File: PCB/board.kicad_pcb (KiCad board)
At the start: 2 copper layers, 161 parts, among them J1 Micro_SD_Card, J10 Conn_01x10, J11 Conn_01x02, J12 Conn_02x04_Odd_Even, J13 Conn_01x02, J14 Conn_01x02, J15 Conn_01x03, J16 Conn_01x02, J17 Conn_01x05, J18 Conn_01x04, J19 Conn_01x04, J2 Conn_ARM_JTAG_SWD_10, J20 Conn_01x02, J21 Conn_01x03, J22 Conn_02x04_Odd_Even, J23 Conn_01x04, J24 Conn_01x04, J25 Conn_01x02, J26 Conn_01x03, J27 Conn_02x04_Odd_Even, J28 Conn_01x04, J29 Conn_01x04, J3 USB_C_Receptacle_USB2.0_14P, J30 Conn_01x02, J31 Conn_01x03, J32 Conn_01x02, J33 Conn_01x02, J34 Conn_01x02, J35 Conn_01x02, J36 Conn_01x02, J37 Conn_01x02, J4 Conn_01x04, J5 Conn_01x04, J6 Conn_01x02, J7 Conn_01x03, J8 Conn_02x04_Odd_Even, J9 Conn_01x10, Q1 IRLML6402, Q2 NMOS, Q3 NMOS, Q4 NMOS, Q5 NMOS, Q6 NMOS, SW1 SW_Push, SW2 SW_Push, U1 STM32H743VITx, U2 AP7361C, U4 TMC Stepstick, U5 TMC Stepstick, U6 TMC Stepstick, U7 TMC Stepstick, U8 AP63203WU, Y2 25 MHz

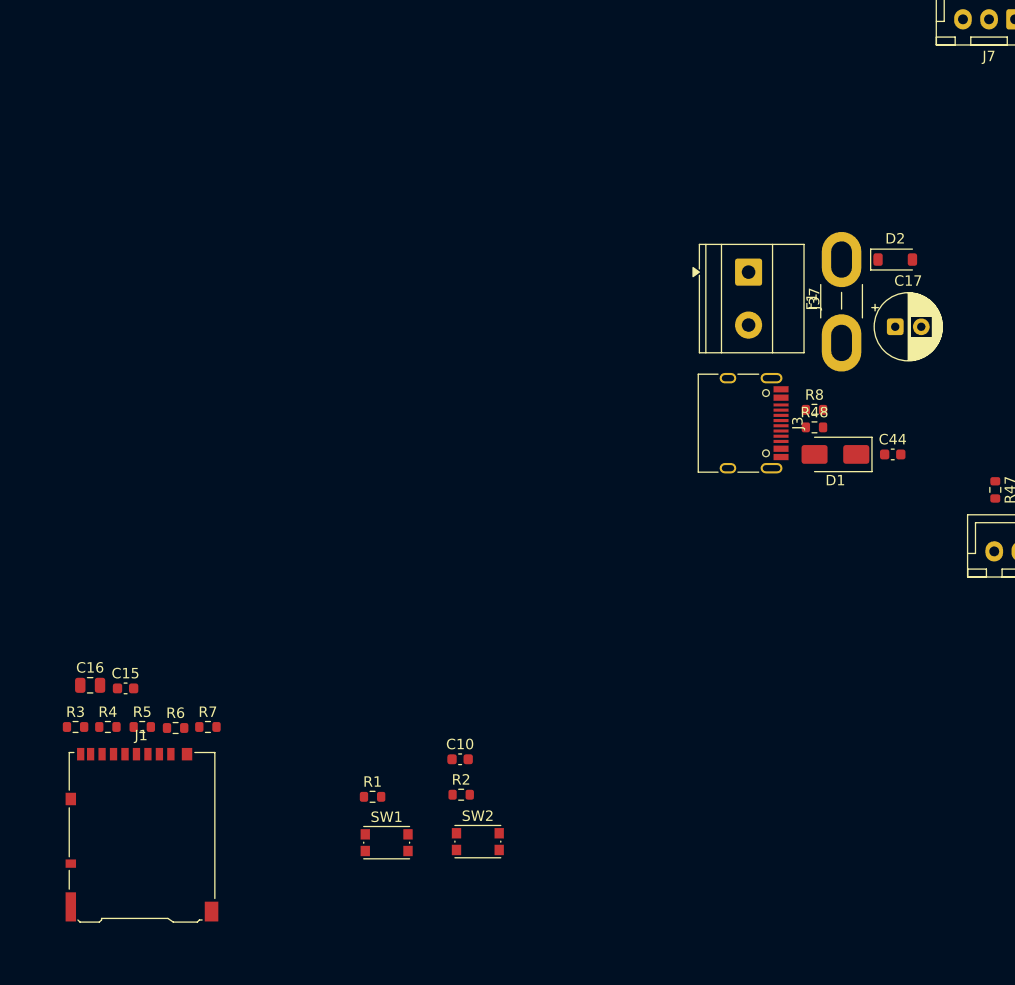
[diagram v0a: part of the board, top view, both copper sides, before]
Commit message: much better organization of the pcb
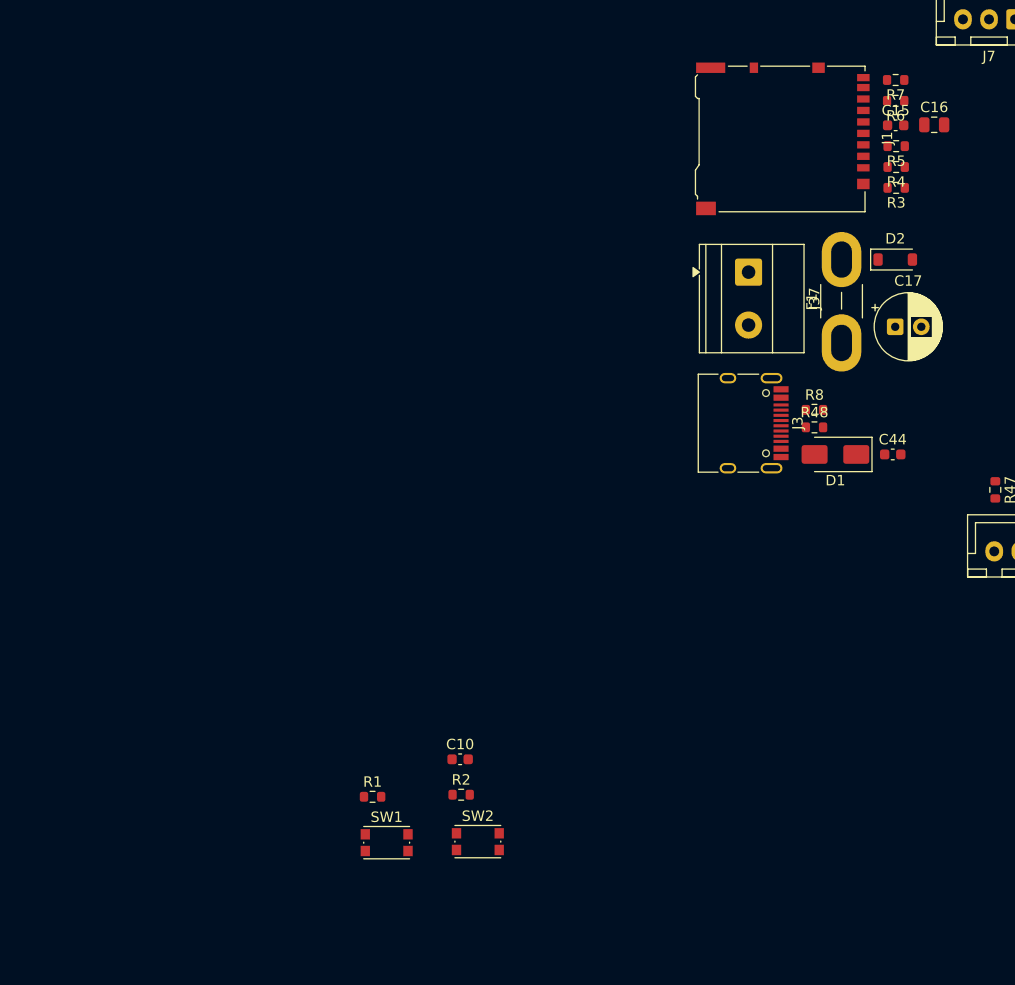
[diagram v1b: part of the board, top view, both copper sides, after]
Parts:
- moved C16 97.2 mm to (159.0, 80.0)
- moved R3 94.2 mm to (155.3, 86.1), turned to 180 degrees
- moved R4 92.8 mm to (155.3, 84.1), turned to 180 degrees
- moved R6 91.6 mm to (155.3, 77.7), turned to 180 degrees
- moved C15 91.5 mm to (155.3, 80.1)
- moved R5 91.3 mm to (155.3, 82.1), turned to 180 degrees
- moved J1 90.8 mm to (144.5, 81.4), turned to -90 degrees
- moved R7 90.6 mm to (155.3, 75.7), turned to 180 degrees

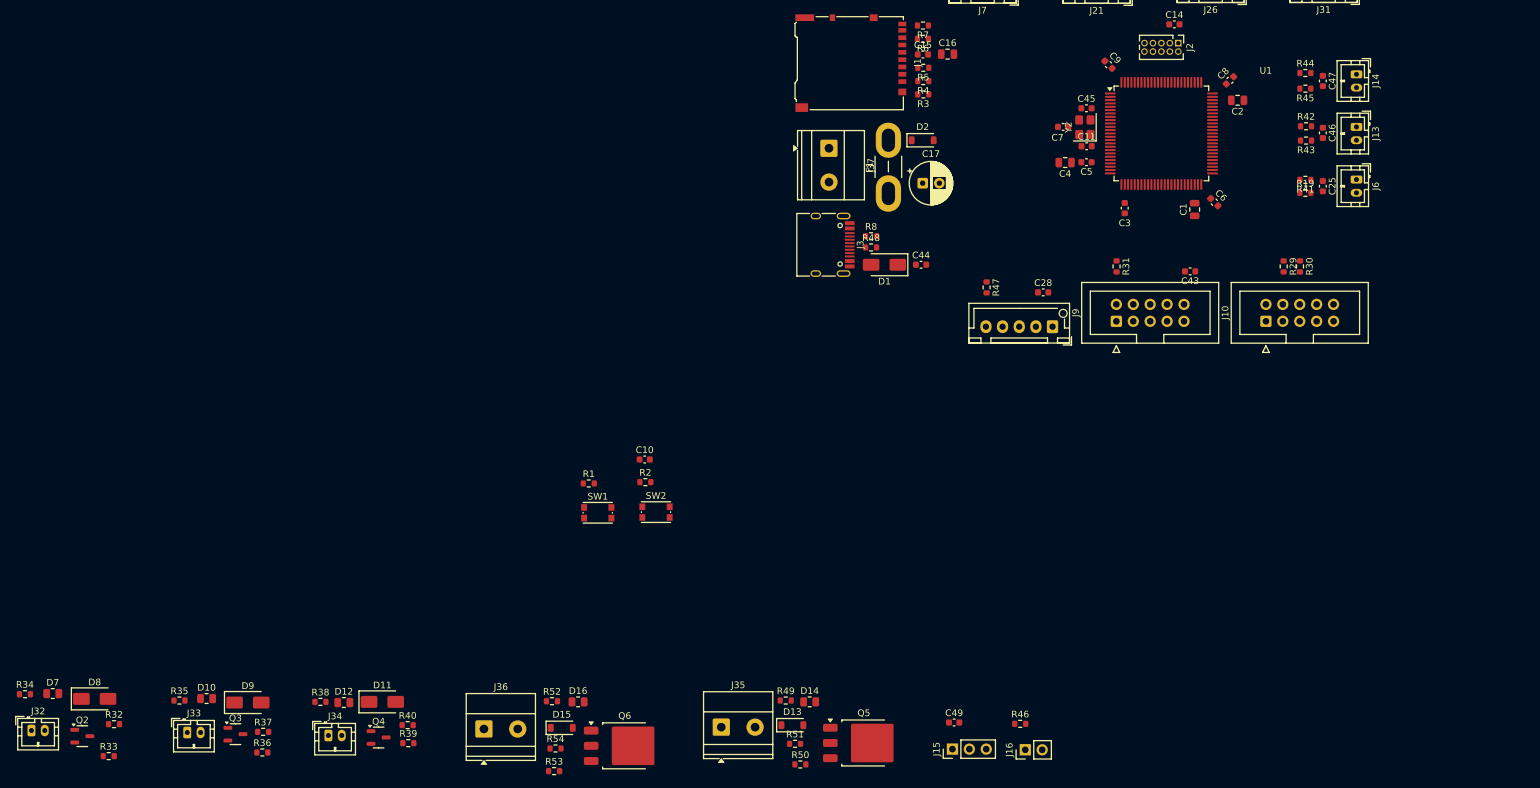
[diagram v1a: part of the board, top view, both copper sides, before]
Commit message: organized fan connectors
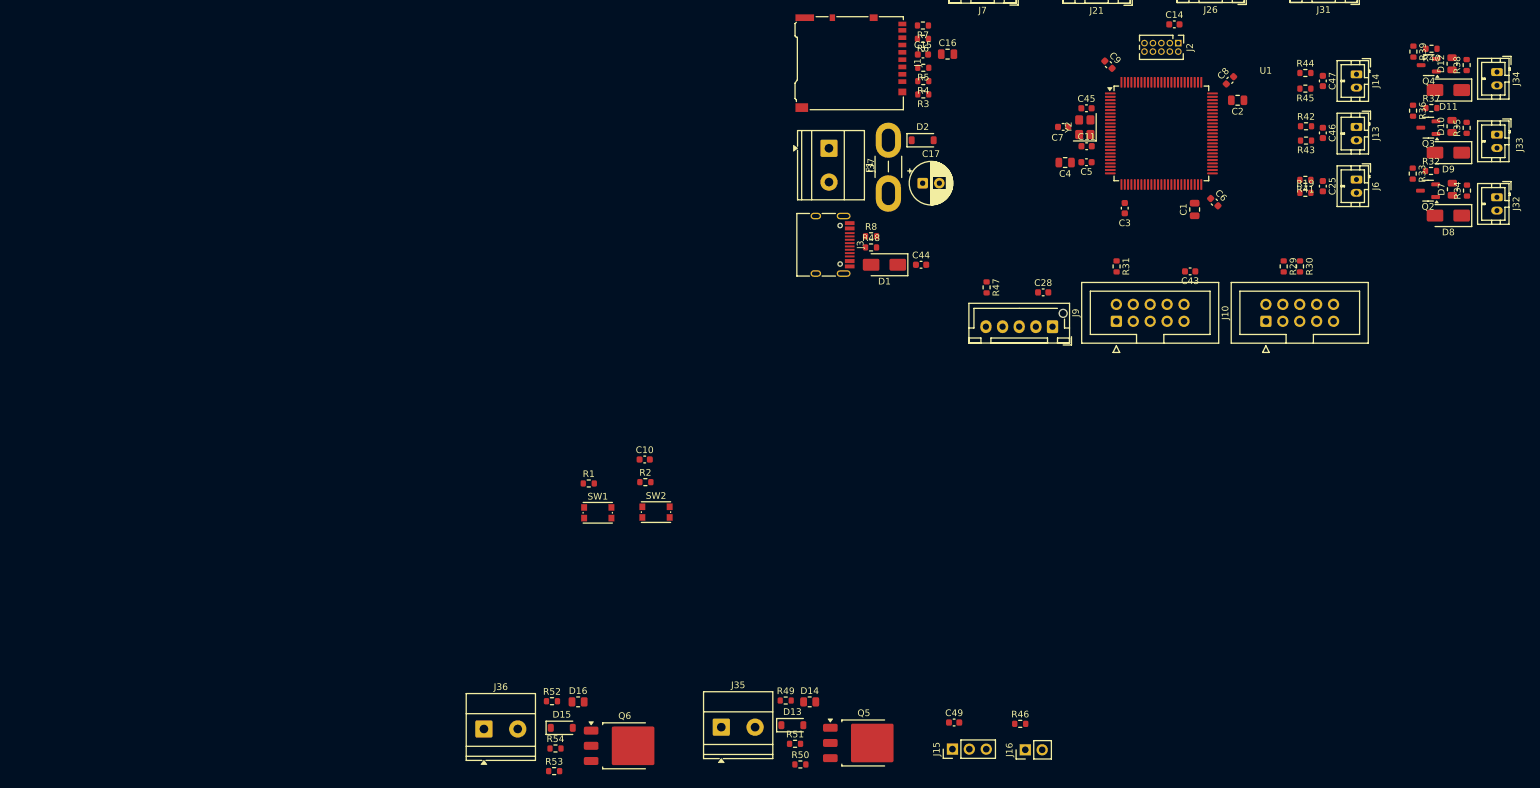
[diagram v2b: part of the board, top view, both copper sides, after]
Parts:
- moved J32 234.2 mm to (241.5, 101.5), turned to -90 degrees
- moved R34 229.4 mm to (237.0, 100.5), turned to 90 degrees
- moved D7 223.4 mm to (234.8, 100.3), turned to 90 degrees
- moved Q2 218.1 mm to (231.2, 100.5), turned to 180 degrees
- moved J33 216.2 mm to (241.5, 92.1), turned to -90 degrees
- moved D8 215.9 mm to (234.2, 104.3), turned to 180 degrees
- moved R32 214.5 mm to (231.6, 97.6)
- moved R33 214.5 mm to (228.8, 98.0), turned to -90 degrees
- moved R35 211.6 mm to (236.9, 91.1), turned to 90 degrees
- moved D10 205.8 mm to (234.8, 90.9), turned to 90 degrees
- moved J34 201.8 mm to (241.5, 82.7), turned to -90 degrees
- moved Q3 201.0 mm to (231.2, 91.1), turned to 180 degrees
- moved R37 198.9 mm to (231.7, 88.1)
- moved D9 198.3 mm to (234.2, 94.8), turned to 180 degrees
- moved R36 197.9 mm to (228.9, 88.5), turned to -90 degrees
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
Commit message: heaters
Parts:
- D13: footprint Diode_SMD:D_SOD-123 -> Diode_SMD:D_SMA
- D15: footprint Diode_SMD:D_SOD-123 -> Package_TO_SOT_SMD:TO-263-2
- moved SW1 76.2 mm to (170.7, 107.8)
- moved C10 71.6 mm to (174.8, 103.8), turned to -90 degrees
- moved SW2 71.5 mm to (170.7, 103.8)
- moved R1 71.4 mm to (165.9, 107.2), turned to 180 degrees
- moved R2 66.7 mm to (165.9, 103.0)
- moved Q6 38.6 mm to (91.8, 150.1), turned to 90 degrees
- moved R53 30.7 mm to (93.2, 157.8)
- moved R54 28.3 mm to (90.3, 157.8)
- moved Q5 19.2 mm to (137.4, 166.5), turned to 90 degrees
- moved D16 19.1 mm to (84.5, 174.7), turned to 180 degrees
- moved D15 18.2 mm to (91.9, 165.4), turned to 90 degrees
- moved R52 14.9 mm to (85.5, 172.2), turned to -90 degrees
- moved R50 10.4 mm to (139.3, 176.6)
- moved R51 10.0 mm to (139.2, 174.1), turned to 180 degrees
- moved J35 8.30 mm to (132.9, 183.5)
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
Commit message: all components place all organized
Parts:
- moved J36 188.9 mm to (269.3, 123.9), turned to 90 degrees
- moved D16 183.9 mm to (262.6, 128.7), turned to -90 degrees
- moved R52 180.2 mm to (260.1, 127.8), turned to 0 degrees
- moved D15 167.4 mm to (253.3, 121.3), turned to 180 degrees
- moved R54 159.3 mm to (245.7, 123.0), turned to 90 degrees
- moved R53 157.1 mm to (245.7, 120.0), turned to 90 degrees
- moved J35 154.1 mm to (269.3, 111.7), turned to 90 degrees
- moved Q6 149.0 mm to (238.0, 121.5), turned to 180 degrees
- moved R49 143.7 mm to (262.3, 109.3), turned to 90 degrees
- moved R50 142.1 mm to (262.3, 105.4), turned to 90 degrees
- moved D13 141.6 mm to (259.5, 113.0), turned to 180 degrees
- moved J15 140.8 mm to (237.9, 67.3), turned to 180 degrees
- moved D14 140.6 mm to (260.1, 109.1), turned to 90 degrees
- moved C49 138.9 mm to (234.9, 63.4), turned to -90 degrees
- moved R51 138.8 mm to (259.9, 105.4), turned to -90 degrees
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
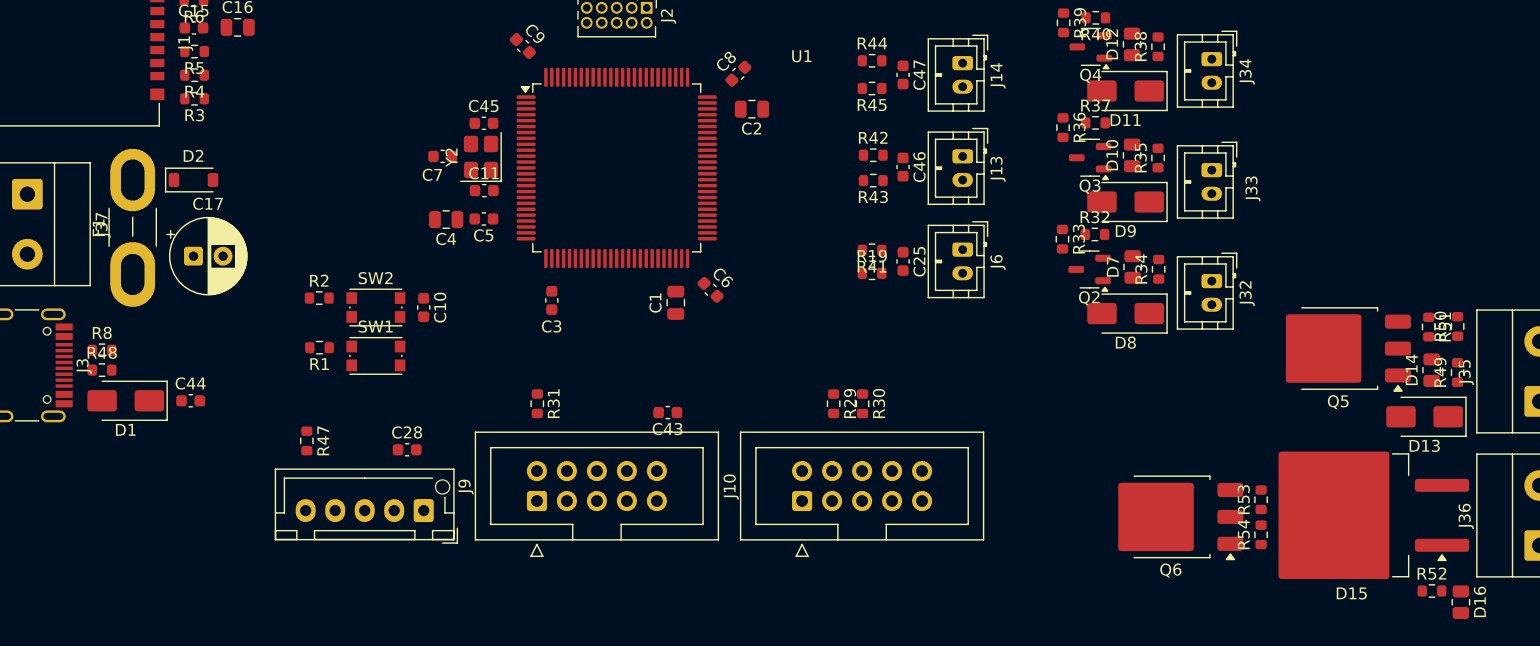
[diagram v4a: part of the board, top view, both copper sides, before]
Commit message: added the organization stuff to the journal
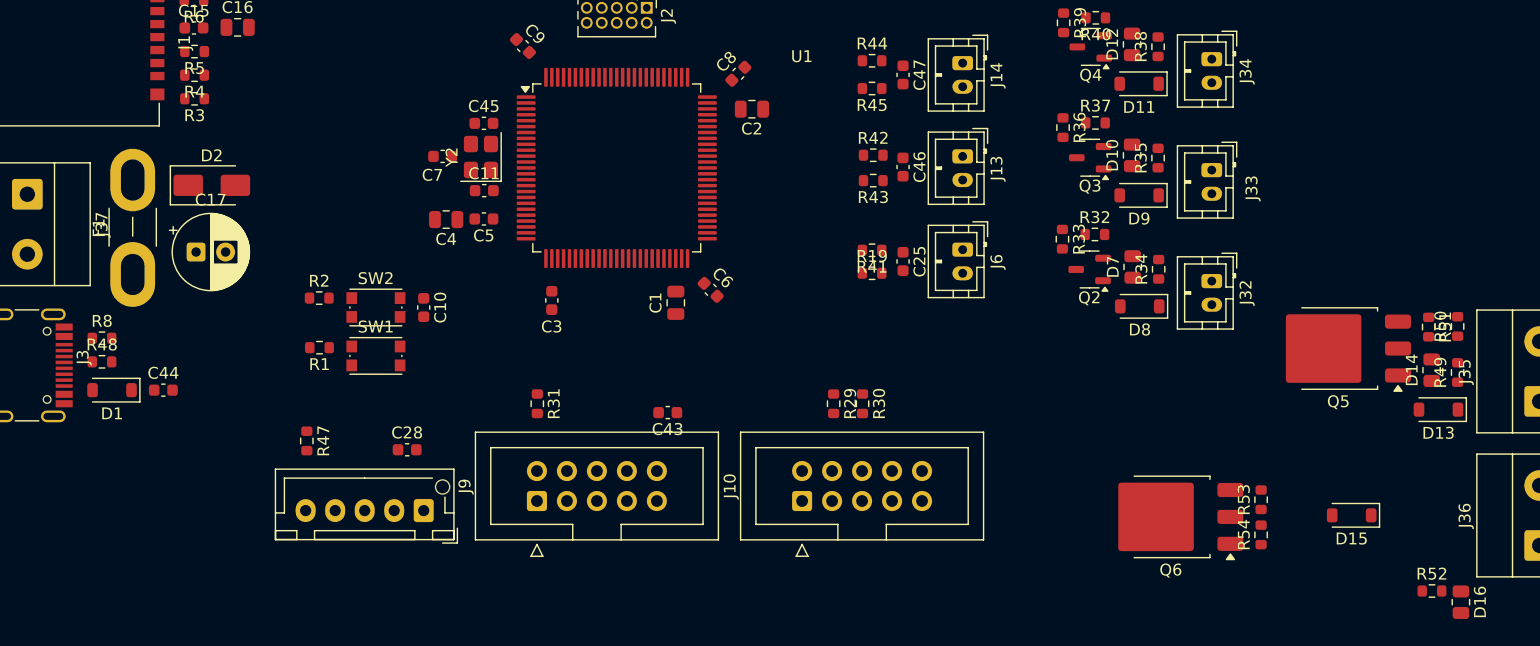
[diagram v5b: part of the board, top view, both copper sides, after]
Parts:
- D1, D11, D13, D8, D9: footprint Diode_SMD:D_SMA -> Diode_SMD:D_SOD-123
- D15: footprint Package_TO_SOT_SMD:TO-263-2 -> Diode_SMD:D_SOD-123
- D2: footprint Diode_SMD:D_SOD-123 -> Diode_SMD:D_SMA
- moved C44 2.48 mm to (152.7, 110.8)
- moved D2 1.61 mm to (156.8, 93.4)
- moved D1 1.47 mm to (148.3, 110.8)
- moved D8 1.35 mm to (235.4, 103.7)
- moved D13 1.32 mm to (260.7, 112.4)
- moved D11 1.30 mm to (235.3, 84.8)
- moved D9 1.28 mm to (235.3, 94.2)
- moved R8 1.02 mm to (147.5, 106.3)
- moved R48 0.70 mm to (147.5, 108.3)
- moved C17 0.41 mm to (155.5, 99.0)

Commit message: organized even BETTER
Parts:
- moved R53 16.7 mm to (262.3, 118.5)
- moved R54 14.9 mm to (259.9, 118.5)
- moved Q6 14.3 mm to (252.2, 119.9)
- moved D15 8.03 mm to (260.7, 124.6)
- moved D16 7.43 mm to (260.1, 121.7)
- moved R52 6.23 mm to (262.3, 121.9), turned to 90 degrees
- moved Q3 2.94 mm to (230.4, 93.9)
- moved R37 2.94 mm to (230.9, 91.0)
- moved R36 2.94 mm to (228.1, 91.3)
- moved Q4 2.89 mm to (230.4, 84.5)
- moved R39 2.89 mm to (228.2, 82.4)
- moved Q2 2.86 mm to (230.5, 103.3)
- moved R32 2.86 mm to (230.9, 100.3)
- moved R33 2.86 mm to (228.2, 100.8)
- moved R40 2.41 mm to (230.9, 81.5)
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
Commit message: re-oriented, this is a good version to go to
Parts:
- moved J15 19.1 mm to (231.3, 49.3)
- moved J16 19.1 mm to (231.3, 56.4)
- moved R46 19.1 mm to (228.3, 55.6)
- moved C49 19.1 mm to (228.3, 45.5)
- moved J34 18.2 mm to (257.1, 73.4)
- moved R35 18.2 mm to (252.6, 81.8)
- moved J32 18.2 mm to (257.1, 92.2)
- moved J33 18.2 mm to (257.1, 82.8)
- moved Q4 18.2 mm to (246.1, 75.2)
- moved R32 18.2 mm to (246.6, 91.0)
- moved R33 18.2 mm to (243.8, 91.5)
- moved R38 18.2 mm to (252.6, 72.4)
- moved R42 18.2 mm to (228.4, 81.5)
- moved R43 18.2 mm to (228.4, 83.7)
- moved D12 18.2 mm to (250.3, 72.2)
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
